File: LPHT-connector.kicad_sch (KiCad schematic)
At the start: 1 part, among them J7 LPHT-04-16-L-RT1-GP

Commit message: chore: more cleanup
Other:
- company: (none) -> Davide, Evan
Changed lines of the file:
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@@
 	(generator_version "9.0")
 	(paper "A4")
+	(title_block
+		(date "2025-11-18")
+		(company "Davide, Evan")
+	)
 	(text "9-16 lan\n"
 		(exclude_from_sim no)
@@
 		)
 	)
-	(global_label "Battery_Out_3.3V"
-		(shape output)
-		(at 205.74 76.2 180)
-		(fields_autoplaced yes)
-		(effects
-			(font
-				(size 1.27 1.27)
-			)
-			(justify right)
-		)
-		(property "Intersheetrefs" "${INTERSHEET_REFS}"
-			(at 186.7892 76.2 0)
-			(effects
-				(font
-					(size 1.27 1.27)
-				)
-				(justify right)
-				(hide yes)
-			)
-		)
-	)
 	(global_label "STM_TX"
 		(shape output)
@@
 	(hierarchical_label "Battery_Out_3.3V"
 		(shape output)
-		(at 205.74 73.66 180)
-		(effects
-			(font
+		(at 205.74 76.2 180)
+		(effects
+			(font

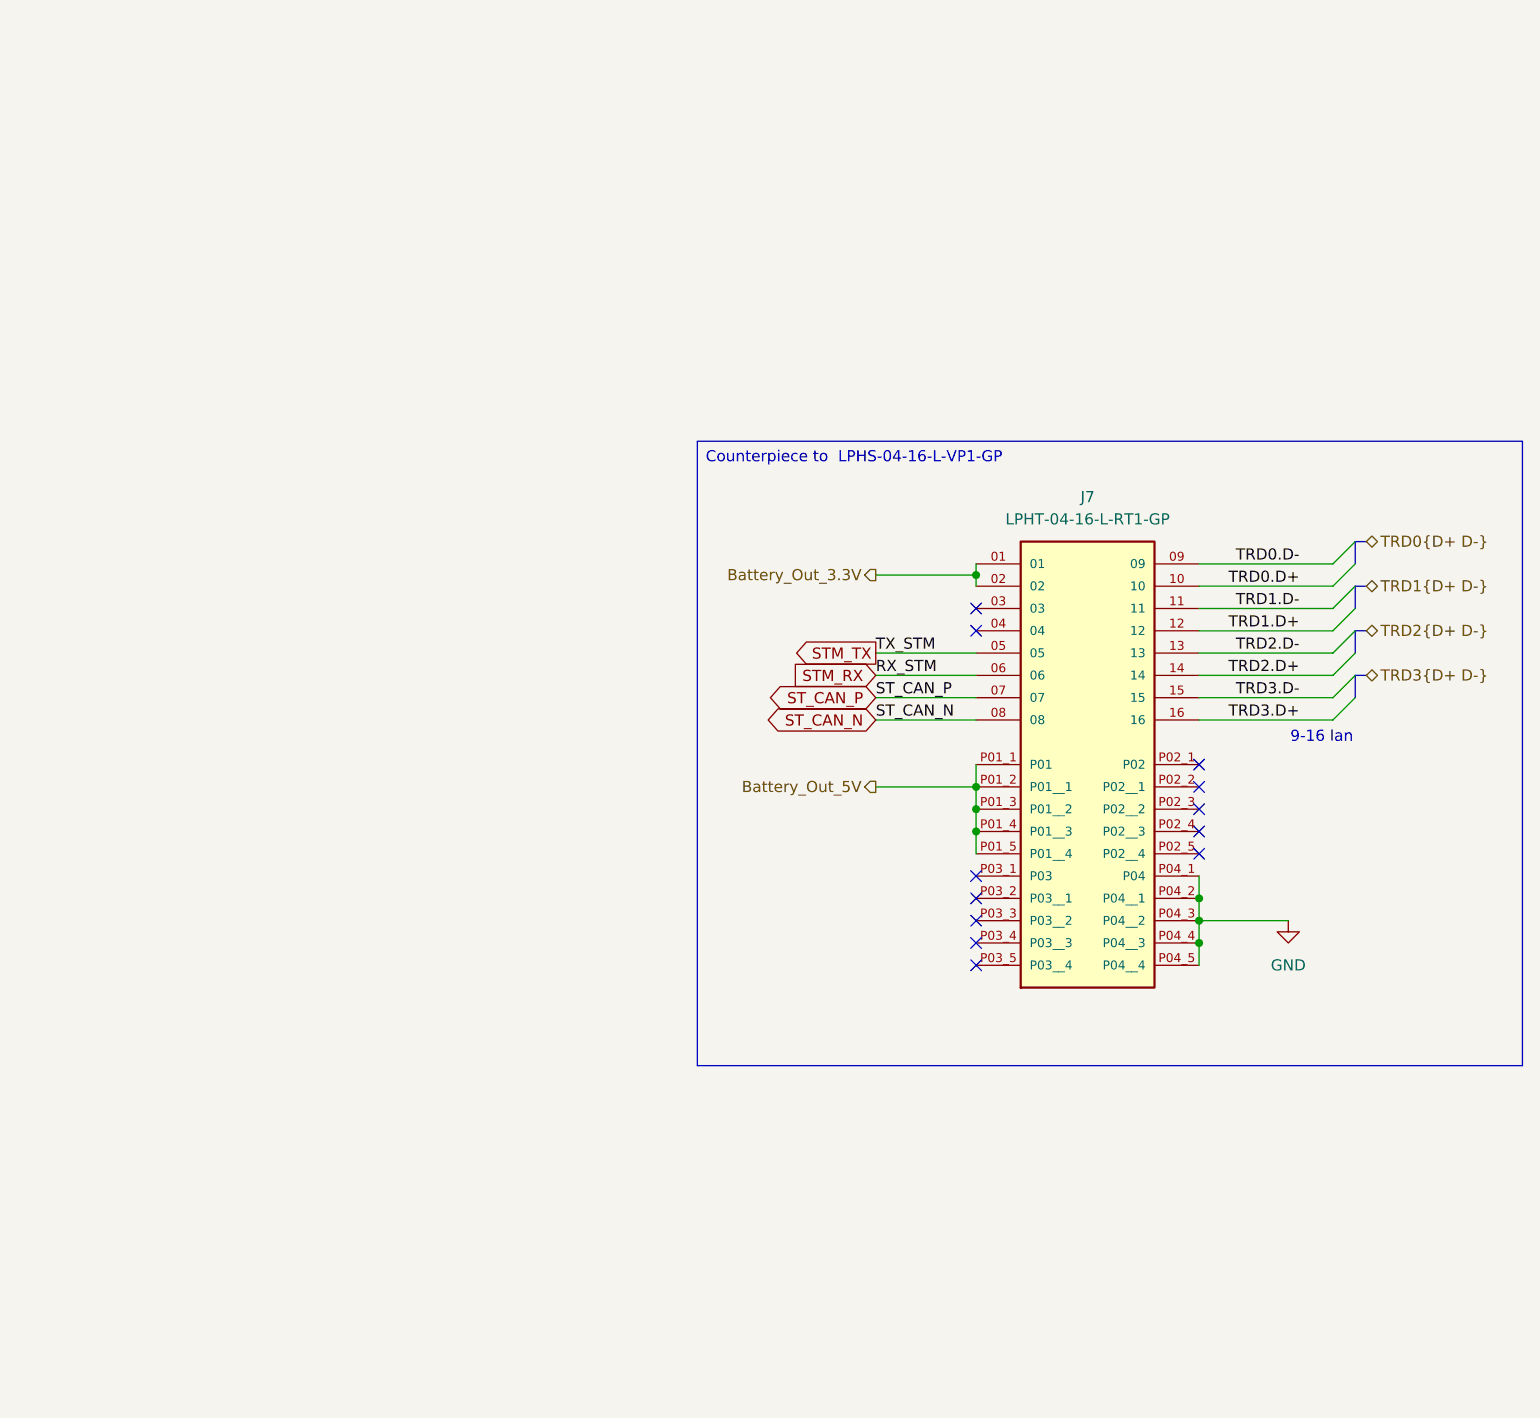
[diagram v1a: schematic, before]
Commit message: chore: added LED indicators for power and activity status, updated symbold, rerouted some things for better visibility
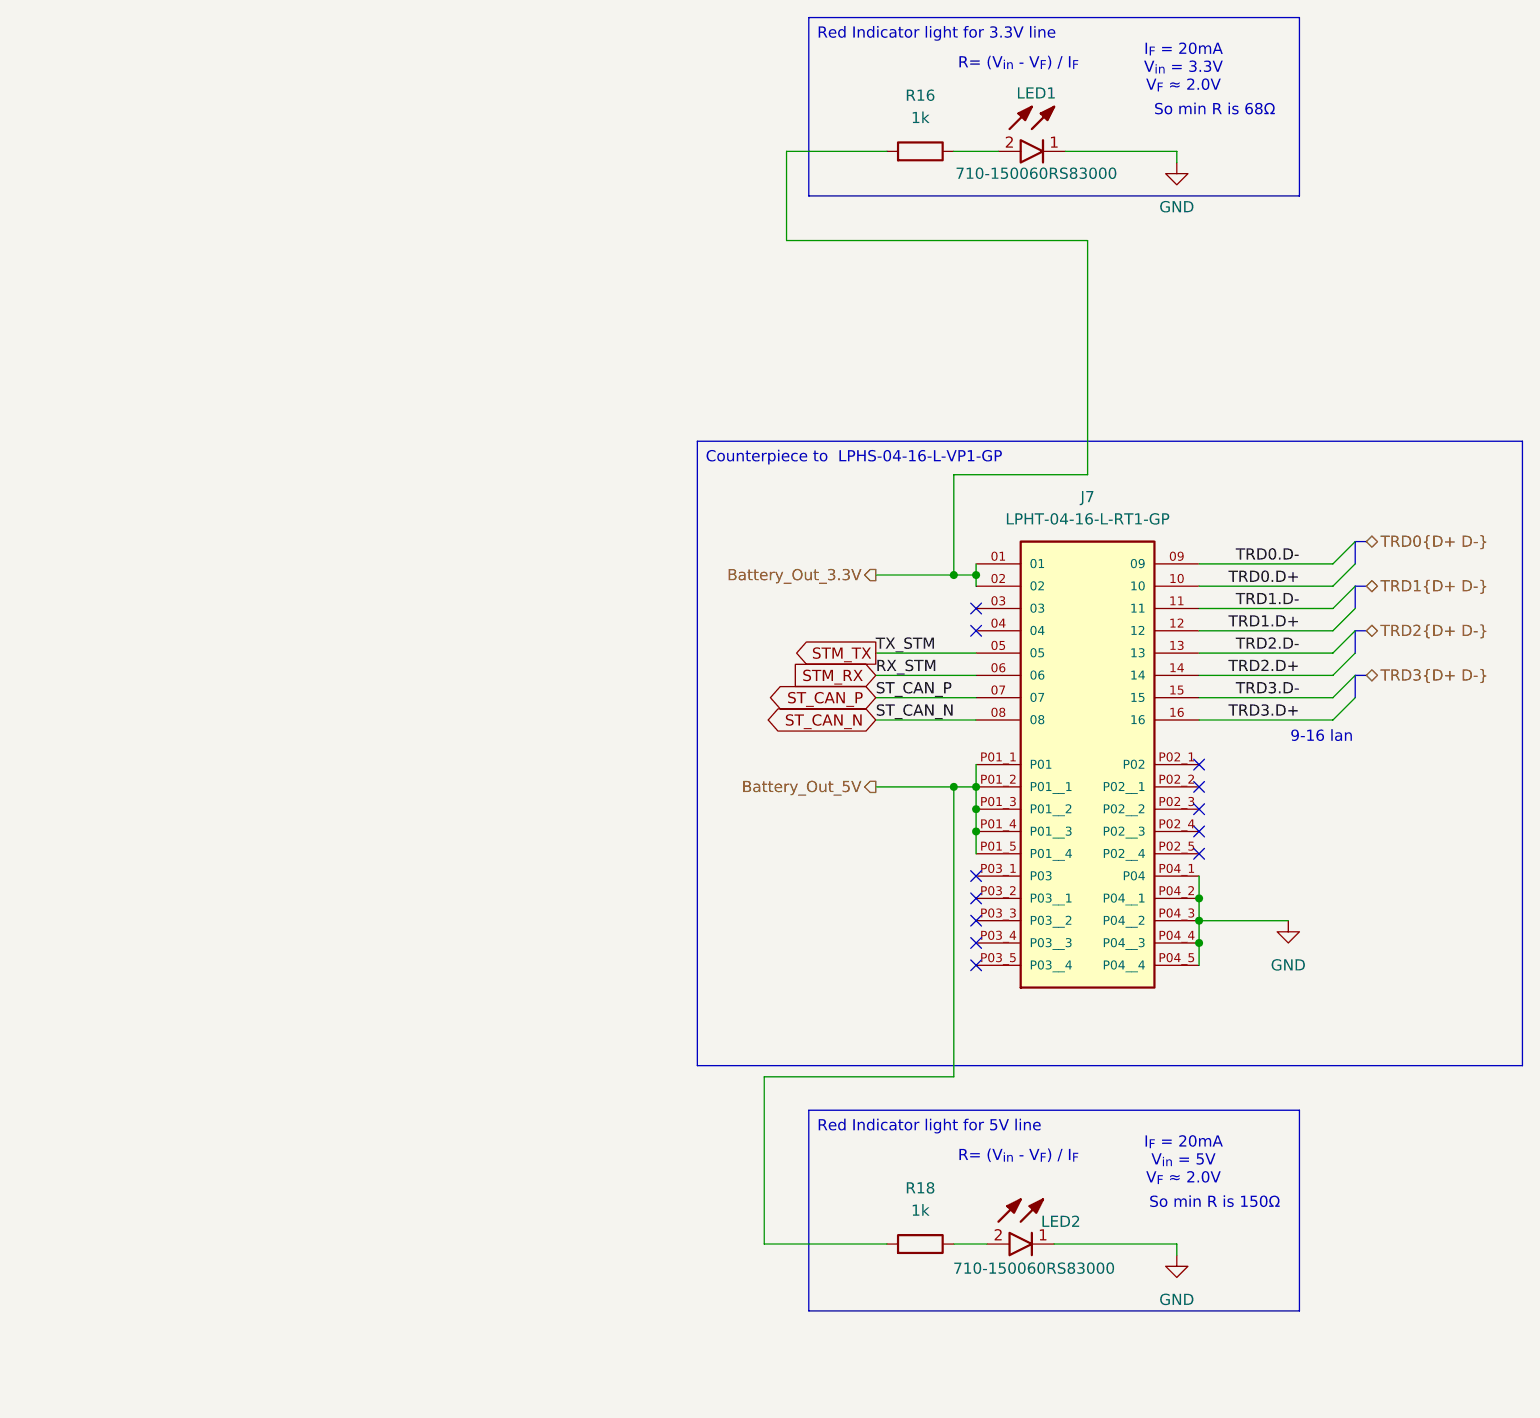
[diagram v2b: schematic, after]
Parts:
- added LED1, LED2: 710-150060RS83000, dz_dio:Wuerth_LED_150060RS83000, symbol #dzdb:s_dio/D-WURT-710-150060RS83000
- added R16, R18: 1k, Resistor_SMD:R_0603_1608Metric, symbol #dzdb:g_res/R-1k-0603
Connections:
- net Battery_Out_3.3V: now also R16.2
- net Battery_Out_5V: now also R18.2
- net GND: now also LED1.1 (K), LED2.1 (K)
- new net: LED2.2 (A), R18.1
- new net: LED1.2 (A), R16.1
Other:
- note added: "I_{F} = 20mA V_{in} = 3.3V V_{F} ≈ 2.0V"
- note added: "I_{F} = 20mA V_{in} = 5V V_{F} ≈ 2.0V"
- note added: "R= (V_{in} - V_{F}) / I_{F}"
- note added: "So min R is 150Ω"
- note added: "So min R is 68Ω"

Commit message: chore: Loads of redoing stuff. Added a Changelog
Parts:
- added D1: 710-82402374, Package_TO_SOT_SMD:SOT-23-5, symbol #dzdb:s_dio/WURT-710-82402374
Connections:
- net Battery_Out_3.3V: now also D1.3 (K)
- net Battery_Out_5V: now also D1.1 (K)
- net GND: now also D1.2 (A)
- net STM_RX renamed STM.RX
- net STM_TX renamed STM.TX
- net ST_CAN_N renamed ST_CAN.N
- net ST_CAN_P renamed ST_CAN.P
- no-connect marks 12 -> 14
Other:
- title: (none) -> Nautilus_Mainboard
- moved on the sheet: J7, LED1, LED2, R16, R18

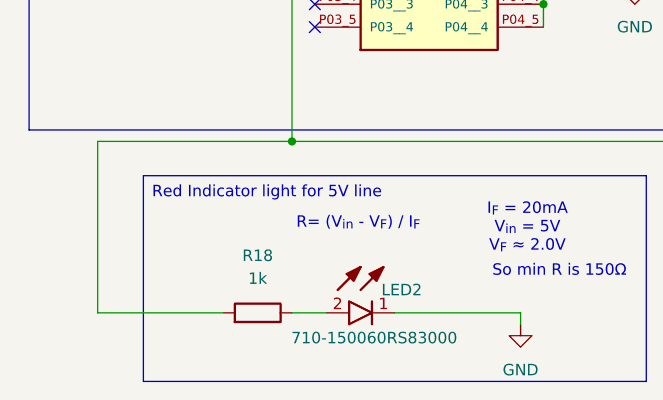
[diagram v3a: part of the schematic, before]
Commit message: feat: added a lot of traces in PCB
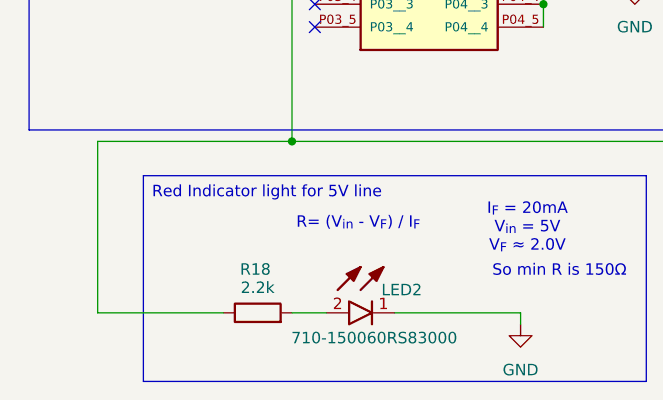
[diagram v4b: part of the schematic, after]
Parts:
- removed R18: 1k, Resistor_SMD:R_0603_1608Metric, symbol #dzdb:g_res/R-1k-0603
- added R18: 2.2k, Resistor_SMD:R_0603_1608Metric, symbol #dzdb:g_res/R-2.2k-0603
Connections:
- net Battery_Out_5V: now also R18.1
- net at LED2.2 (A): now also R18.2
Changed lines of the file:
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@@
+	)
+	(symbol
+		(lib_id "#dzdb:g_res/R-2.2k-0603")
+		(at 134.62 162.56 90)
+		(unit 1)
+		(exclude_from_sim no)
+		(in_bom yes)
+		(on_board yes)
+		(dnp no)
+		(property "Reference" "R18"
+			(at 134.366 157.734 90)
+			(effects
+				(font
+					(size 1.27 1.27)
+				)
+			)
+		)
+		(property "Value" "2.2k"
+			(at 134.62 159.766 90)
+			(effects
+				(font
+					(size 1.27 1.27)
+				)
+			)
+		)
+		(property "Footprint" "Resistor_SMD:R_0603_1608Metric"
+			(at 134.62 164.338 90)
+			(effects
+				(font
+					(size 1.27 1.27)
+				)
+				(hide yes)
+			)
+		)
+		(property "Datasheet" "https://www.we-online.com/components/products/datasheet/560112116098.pdf"
+			(at 134.62 162.56 0)
+			(effects
+				(font
+					(size 1.27 1.27)
+				)
+				(hide yes)
+			)
+		)
+		(property "Description" "Thick Film Resistors - SMD WRIS-RSKS 2.2 kOhms 1 % 0.1 W 0603"
+			(at 134.62 162.56 0)
+			(effects
+				(font
+					(size 1.27 1.27)
+				)
+				(hide yes)
+			)
+		)
+		(property "IPN" "R-2.2k-0603"
+			(at 134.62 162.56 0)
+			(effects
+				(font
+					(size 1.27 1.27)
+				)
+				(hide yes)
+			)
+		)
+		(property "MPN" "560112116098"
+			(at 134.62 162.56 0)
+			(effects
+				(font
+					(size 1.27 1.27)
+				)
+				(hide yes)
+			)
+		)
+		(property "Manufacturer" "Wurth Elektronik"
+			(at 134.62 162.56 0)
+			(effects
+				(font
+					(size 1.27 1.27)
+				)
+				(hide yes)
+			)
+		)
+		(property "Resistance" "2.2k"
+			(at 134.62 162.56 0)
+			(effects
+				(font
+					(size 1.27 1.27)
+				)
+				(hide yes)
+			)
+		)
+		(property "Power" "0.1 W"
+			(at 134.62 162.56 0)
+			(effects
+				(font
+					(size 1.27 1.27)
+				)
+				(hide yes)
+			)
+		)
+		(property "Material" "Thick film"
+			(at 134.62 162.56 0)
+			(effects
+				(font
+					(size 1.27 1.27)
+				)
+				(hide yes)
+			)
+		)
+		(property "Tolerance" "1 %"
+			(at 134.62 162.56 0)
+			(effects
+				(font
+					(size 1.27 1.27)
+				)
+				(hide yes)
+			)
+		)
+		(property "Supplier" "Mouser"
+			(at 134.62 162.56 0)
+			(effects
+				(font
+					(size 1.27 1.27)
+				)
+				(hide yes)
+			)
+		)
+		(property "SPN" "710-560112116098"
+			(at 134.62 162.56 0)
+			(effects
+				(font
+					(size 1.27 1.27)
+				)
+				(hide yes)
+			)
+		)
+		(property "LCSC" "CXXXXX"
+			(at 134.62 162.56 0)
+			(effects
+				(font
+					(size 1.27 1.27)
+				)
+				(hide yes)
+			)
+		)
+		(property "Comment" "lifecycle=Active; note=Auto-generated"
+			(at 134.62 162.56 0)
+			(effects
+				(font
+					(size 1.27 1.27)
+				)
+				(hide yes)
+			)
+		)
+		(pin "1"
+		)
+		(pin "2"
+		)
+		(instances
+			(project ""
+				(path "/ce1819b2-f280-40ed-834f-6fe4d12f809d/8ca810bd-6311-4873-a4c4-10e0b1989f7a"
+					(reference "R18")
+					(unit 1)
+				)
+			)
+		)
 	)
 	(symbol
@@
 					(unit 1)
 				)
-			)
-		)
-	)
-	(symbol
-		(lib_id "#dzdb:g_res/R-1k-0603")
-		(at 134.62 162.56 270)
-		(mirror x)
-		(unit 1)
-		(exclude_from_sim no)
-		(in_bom yes)
-		(on_board yes)
-		(dnp no)
-		(fields_autoplaced yes)
-		(property "Reference" "R18"
-			(at 134.62 156.21 90)
-			(effects
-				(font
-					(size 1.27 1.27)
-				)
-			)
-		)
-		(property "Value" "1k"
-			(at 134.62 158.75 90)
-			(effects
-				(font
-					(size 1.27 1.27)
-				)
-			)
-		)
-		(property "Footprint" "Resistor_SMD:R_0603_1608Metric"
-			(at 134.62 164.338 90)
-			(effects
-				(font
-					(size 1.27 1.27)
-				)
-				(hide yes)
-			)
-		)
-		(property "Datasheet" "https://www.we-online.com/components/products/datasheet/560112116014.pdf"
-			(at 134.62 162.56 0)
-			(effects
-				(font
-					(size 1.27 1.27)
-				)
-				(hide yes)
-			)
-		)
-		(property "Description" "Thick Film Resistors - SMD WRIS-RSKS 1 kOhms 1 % 0.1 W 0603"
-			(at 134.62 162.56 0)
-			(effects
-				(font
-					(size 1.27 1.27)
-				)
-				(hide yes)
-			)
-		)
-		(property "IPN" "R-1k-0603"
-			(at 134.62 162.56 0)
-			(effects
-				(font
-					(size 1.27 1.27)
-				)
-				(hide yes)
-			)
-		)
-		(property "MPN" "560112116014"
-			(at 134.62 162.56 0)
-			(effects
-				(font
-					(size 1.27 1.27)
-				)
-				(hide yes)
-			)
-		)
-		(property "Manufacturer" "Wurth Elektronik"
-			(at 134.62 162.56 0)
-			(effects
-				(font
-					(size 1.27 1.27)
-				)
-				(hide yes)
-			)
-		)
-		(property "Resistance" "1k"
-			(at 134.62 162.56 0)
-			(effects
-				(font
-					(size 1.27 1.27)
-				)
-				(hide yes)
-			)
-		)
-		(property "Power" "0.1 W"
-			(at 134.62 162.56 0)
-			(effects
-				(font
-					(size 1.27 1.27)
-				)
-				(hide yes)
-			)
-		)
-		(property "Material" "Thick film"
-			(at 134.62 162.56 0)
-			(effects
-				(font
-					(size 1.27 1.27)
-				)
-				(hide yes)
-			)
-		)
-		(property "Tolerance" "1 %"
-			(at 134.62 162.56 0)
-			(effects
-				(font
-					(size 1.27 1.27)
-				)
-				(hide yes)
-			)
-		)
-		(property "Supplier" "Mouser"
-			(at 134.62 162.56 0)
-			(effects
-				(font
-					(size 1.27 1.27)
-				)
-				(hide yes)
-			)
-		)
-		(property "SPN" "710-560112116014"
-			(at 134.62 162.56 0)
-			(effects
-				(font
-					(size 1.27 1.27)
-				)
-				(hide yes)
-			)
-		)
-		(property "LCSC" "CXXXXX"
-			(at 134.62 162.56 0)
-			(effects
-				(font
-					(size 1.27 1.27)
-				)
-				(hide yes)
-			)
-		)
-		(property "Comment" "lifecycle=Active; note=Auto-generated"
-			(at 134.62 162.56 0)
-			(effects
-				(font
-					(size 1.27 1.27)
-				)
-				(hide yes)
-			)
-		)
-		(pin "1"
-		)
-		(pin "2"
-		)
-		(instances
-			(project "nautilus_mainboard"
-				(path "/ce1819b2-f280-40ed-834f-6fe4d12f809d/8ca810bd-6311-4873-a4c4-10e0b1989f7a"
-					(reference "R18")
-					(unit 1)
-				)
